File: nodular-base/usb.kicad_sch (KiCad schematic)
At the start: 39 parts, among them J10 Conn_01x02_MountingPin, J7 USB_C_Receptacle_USB2.0, J8 USB_C_Receptacle_USB2.0, U2 FUSB302BMPX, U29 RCLAMP0524P-ES, U3 BQ25895RTW, U43 TLV62595DMQR, U5 FUSB302BMPX, U50 TS3USB221A

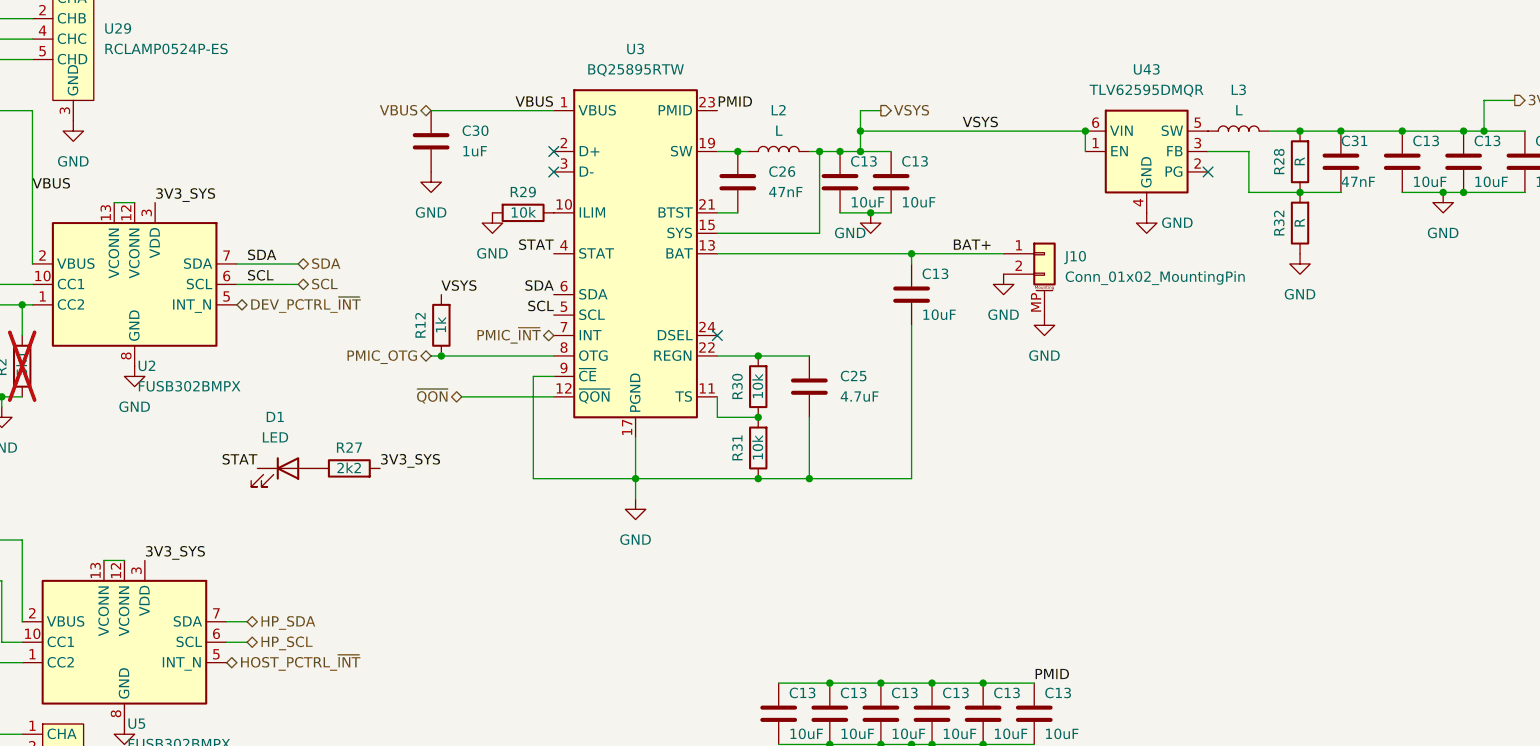
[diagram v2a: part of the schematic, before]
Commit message: Add hole Add decoupling caps, pullups, and voltage dividers Set current limit on PMIC Determine battery attachment angle Update BOM and pinouts
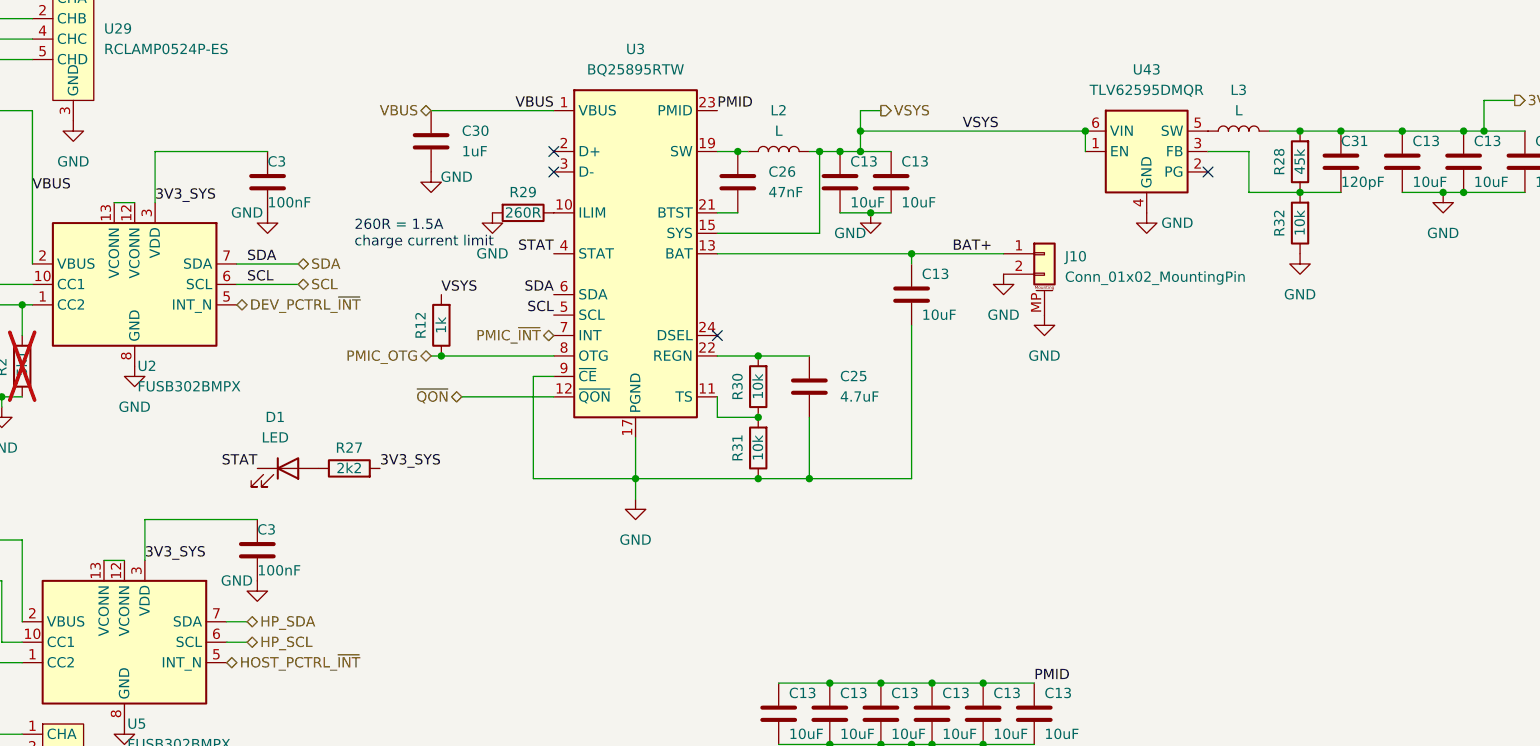
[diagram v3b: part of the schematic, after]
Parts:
- added C3 (x2): 100nF, Capacitor_SMD:C_0402_1005Metric, symbol Device:C
- C31: value 47nF -> 120pF
- J10: footprint JST_PH_B2B-PH-SM4-TB_1x02-1MP_P2.00mm_Vertical -> nodular:JST_PH_B2B-PH-SM4-TB_1x02-1MP_P2.00mm_Vertical
- R28: value R -> 45k
- R29: value 10k -> 260R
- R32: value R -> 10k
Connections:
- net 3V3_SYS: now also C3.1, C3.1
- net GND: now also C3.2, C3.2
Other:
- note added: "260R = 1.5A charge current limit"
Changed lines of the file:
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@@
+    (stroke (width 0) (type default))
+  )
+  (wire (pts (xy 109.22 39.37) (xy 95.25 39.37))
     (stroke (width 0) (type default))
   )
@@
     (stroke (width 0) (type default))
   )
+  (wire (pts (xy 107.95 85.09) (xy 93.98 85.09))
+    (stroke (width 0) (type default))
+  )
   (wire (pts (xy 172.72 113.03) (xy 179.07 113.03))
     (stroke (width 0) (type default))
@@
     (stroke (width 0) (type default))
   )
+  (wire (pts (xy 95.25 39.37) (xy 95.25 45.72))
+    (stroke (width 0) (type default))
+  )
   (wire (pts (xy 182.88 36.83) (xy 210.82 36.83))
     (stroke (width 0) (type default))
@@
     (stroke (width 0) (type default))
   )
+  (wire (pts (xy 93.98 85.09) (xy 93.98 90.17))
+    (stroke (width 0) (type default))
+  )
   (wire (pts (xy 78.74 87.63) (xy 78.74 97.79))
     (stroke (width 0) (type default))
@@
   (wire (pts (xy 107.95 140.97) (xy 110.49 140.97))
     (stroke (width 0) (type default))
+  )
+  (text "260R = 1.5A \ncharge current limit" (at 120.015 51.435 0)
+    (effects (font (size 1.27 1.27)) (justify left bottom))
   )
   (label "SDA" (at 144.78 57.15 180) (fields_autoplaced)
@@
   )
   (symbol (lib_id "power:GND") (at 129.54 41.91 0) (unit 1)
-    (in_bom yes) (on_board yes) (dnp no) (fields_autoplaced)
+    (in_bom yes) (on_board yes) (dnp no)
     (property "Reference" "#PWR045" (at 129.54 48.26 0)
       (effects (font (size 1.27 1.27)) hide)
     )
-    (property "Value" "GND" (at 129.54 46.99 0)
+    (property "Value" "GND" (at 132.715 42.545 0)
       (effects (font (size 1.27 1.27)))
     )
@@
     )
   )
+  (symbol (lib_id "Device:C") (at 109.22 43.18 0) (unit 1)
+    (in_bom yes) (on_board yes) (dnp no)
+    (property "Reference" "C3" (at 109.22 40.64 0)
+      (effects (font (size 1.27 1.27)) (justify left))
+    )
+    (property "Value" "100nF" (at 109.22 45.72 0)
+      (effects (font (size 1.27 1.27)) (justify left))
+    )
+    (property "Footprint" "Capacitor_SMD:C_0402_1005Metric" (at 110.1852 46.99 0)
+      (effects (font (size 1.27 1.27)) hide)
+    )
+    (property "Datasheet" "~" (at 109.22 43.18 0)
+      (effects (font (size 1.27 1.27)) hide)
+    )
+    (pin "1")
+    (pin "2")
+    (instances
+      (project "nodular-base"
+        (path "/6dcb0502-87e2-4c28-9ce8-81aab8925f06"
+          (reference "C3") (unit 1)
+        )
+        (path "/6dcb0502-87e2-4c28-9ce8-81aab8925f06/5ae693f9-48f3-406c-bbdf-b76d81cc71eb"
+          (reference "C16") (unit 1)
+        )
+        (path "/6dcb0502-87e2-4c28-9ce8-81aab8925f06/52c49487-f3d5-40e2-8f19-e7b81498d838"
+          (reference "C44") (unit 1)
+        )
+        (path "/6dcb0502-87e2-4c28-9ce8-81aab8925f06/febeaf27-8aaa-445d-863a-3f8ee5c51d55"
+          (reference "C46") (unit 1)
+        )
+      )
+    )
+  )
+  (symbol (lib_id "power:GND") (at 107.95 92.71 0) (unit 1)
+    (in_bom yes) (on_board yes) (dnp no)
+    (property "Reference" "#PWR064" (at 107.95 99.06 0)
+      (effects (font (size 1.27 1.27)) hide)
+    )
+    (property "Value" "GND" (at 105.41 92.71 0)
+      (effects (font (size 1.27 1.27)))
+    )
+    (property "Footprint" "" (at 107.95 92.71 0)
+      (effects (font (size 1.27 1.27)) hide)
+    )
+    (property "Datasheet" "" (at 107.95 92.71 0)
+      (effects (font (size 1.27 1.27)) hide)
+    )
+    (pin "1")
+    (instances
+      (project "nodular-base"
+        (path "/6dcb0502-87e2-4c28-9ce8-81aab8925f06/52c49487-f3d5-40e2-8f19-e7b81498d838"
+          (reference "#PWR064") (unit 1)
+        )
+        (path "/6dcb0502-87e2-4c28-9ce8-81aab8925f06/febeaf27-8aaa-445d-863a-3f8ee5c51d55"
+          (reference "#PWR067") (unit 1)
+        )
+      )
+    )
+  )
   (symbol (lib_id "Device:C") (at 167.64 43.18 0) (unit 1)
     (in_bom yes) (on_board yes) (dnp no) (fields_autoplaced)
@@
       (effects (font (size 1.27 1.27)))
     )
-    (property "Value" "10k" (at 140.97 46.99 90)
+    (property "Value" "260R" (at 140.97 46.99 90)
       (effects (font (size 1.27 1.27)))
     )
@@
       (effects (font (size 1.27 1.27)) (justify left))
     )
-    (property "Footprint" "JST_PH_B2B-PH-SM4-TB_1x02-1MP_P2.00mm_Vertical" (at 205.74 52.07 0)
+    (property "Footprint" "nodular:JST_PH_B2B-PH-SM4-TB_1x02-1MP_P2.00mm_Vertical" (at 205.74 52.07 0)
       (effects (font (size 1.27 1.27)) hide)
     )
@@
         (path "/6dcb0502-87e2-4c28-9ce8-81aab8925f06/febeaf27-8aaa-445d-863a-3f8ee5c51d55"
           (reference "L2") (unit 1)
+        )
+      )
+    )
+  )
+  (symbol (lib_id "Device:C") (at 107.95 88.9 0) (unit 1)
+    (in_bom yes) (on_board yes) (dnp no)
+    (property "Reference" "C3" (at 107.95 86.36 0)
+      (effects (font (size 1.27 1.27)) (justify left))
+    )
+    (property "Value" "100nF" (at 107.95 91.44 0)
+      (effects (font (size 1.27 1.27)) (justify left))
+    )
+    (property "Footprint" "Capacitor_SMD:C_0402_1005Metric" (at 108.9152 92.71 0)
+      (effects (font (size 1.27 1.27)) hide)
+    )
+    (property "Datasheet" "~" (at 107.95 88.9 0)
+      (effects (font (size 1.27 1.27)) hide)
+    )
+    (pin "1")
+    (pin "2")
+    (instances
+      (project "nodular-base"
+        (path "/6dcb0502-87e2-4c28-9ce8-81aab8925f06"
+          (reference "C3") (unit 1)
+        )
+        (path "/6dcb0502-87e2-4c28-9ce8-81aab8925f06/5ae693f9-48f3-406c-bbdf-b76d81cc71eb"
+          (reference "C16") (unit 1)
+        )
+        (path "/6dcb0502-87e2-4c28-9ce8-81aab8925f06/52c49487-f3d5-40e2-8f19-e7b81498d838"
+          (reference "C44") (unit 1)
+        )
+        (path "/6dcb0502-87e2-4c28-9ce8-81aab8925f06/febeaf27-8aaa-445d-863a-3f8ee5c51d55"
+          (reference "C47") (unit 1)
         )
       )
@@
       (effects (font (size 1.27 1.27)))
     )
-    (property "Value" "R" (at 237.49 40.64 90)
+    (property "Value" "45k" (at 237.49 40.64 90)
       (effects (font (size 1.27 1.27)))
     )
@@
       (effects (font (size 1.27 1.27)))
     )
-    (property "Value" "R" (at 237.49 48.26 90)
+    (property "Value" "10k" (at 237.49 48.26 90)
       (effects (font (size 1.27 1.27)))
     )
@@
     )
   )
+  (symbol (lib_id "power:GND") (at 109.22 46.99 0) (unit 1)
+    (in_bom yes) (on_board yes) (dnp no)
+    (property "Reference" "#PWR064" (at 109.22 53.34 0)
+      (effects (font (size 1.27 1.27)) hide)
+    )
+    (property "Value" "GND" (at 106.68 46.99 0)
+      (effects (font (size 1.27 1.27)))
+    )
+    (property "Footprint" "" (at 109.22 46.99 0)
+      (effects (font (size 1.27 1.27)) hide)
+    )
+    (property "Datasheet" "" (at 109.22 46.99 0)
+      (effects (font (size 1.27 1.27)) hide)
+    )
+    (pin "1")
+    (instances
+      (project "nodular-base"
+        (path "/6dcb0502-87e2-4c28-9ce8-81aab8925f06/52c49487-f3d5-40e2-8f19-e7b81498d838"
+          (reference "#PWR064") (unit 1)
+        )
+        (path "/6dcb0502-87e2-4c28-9ce8-81aab8925f06/febeaf27-8aaa-445d-863a-3f8ee5c51d55"
+          (reference "#PWR066") (unit 1)
+        )
+      )
+    )
+  )
   (symbol (lib_id "Device:C") (at 265.43 40.64 0) (unit 1)
     (in_bom yes) (on_board yes) (dnp no)
@@
       (effects (font (size 1.27 1.27)) (justify left))
     )
-    (property "Value" "47nF" (at 242.57 43.18 0)
-      (effects (font (size 1.27 1.27)) (justify left))
-    )
+    (property "Value" "120pF" (at 242.57 43.18 0)
+      (effects (font (size 1.27 1.27)) (justify left))
+    )

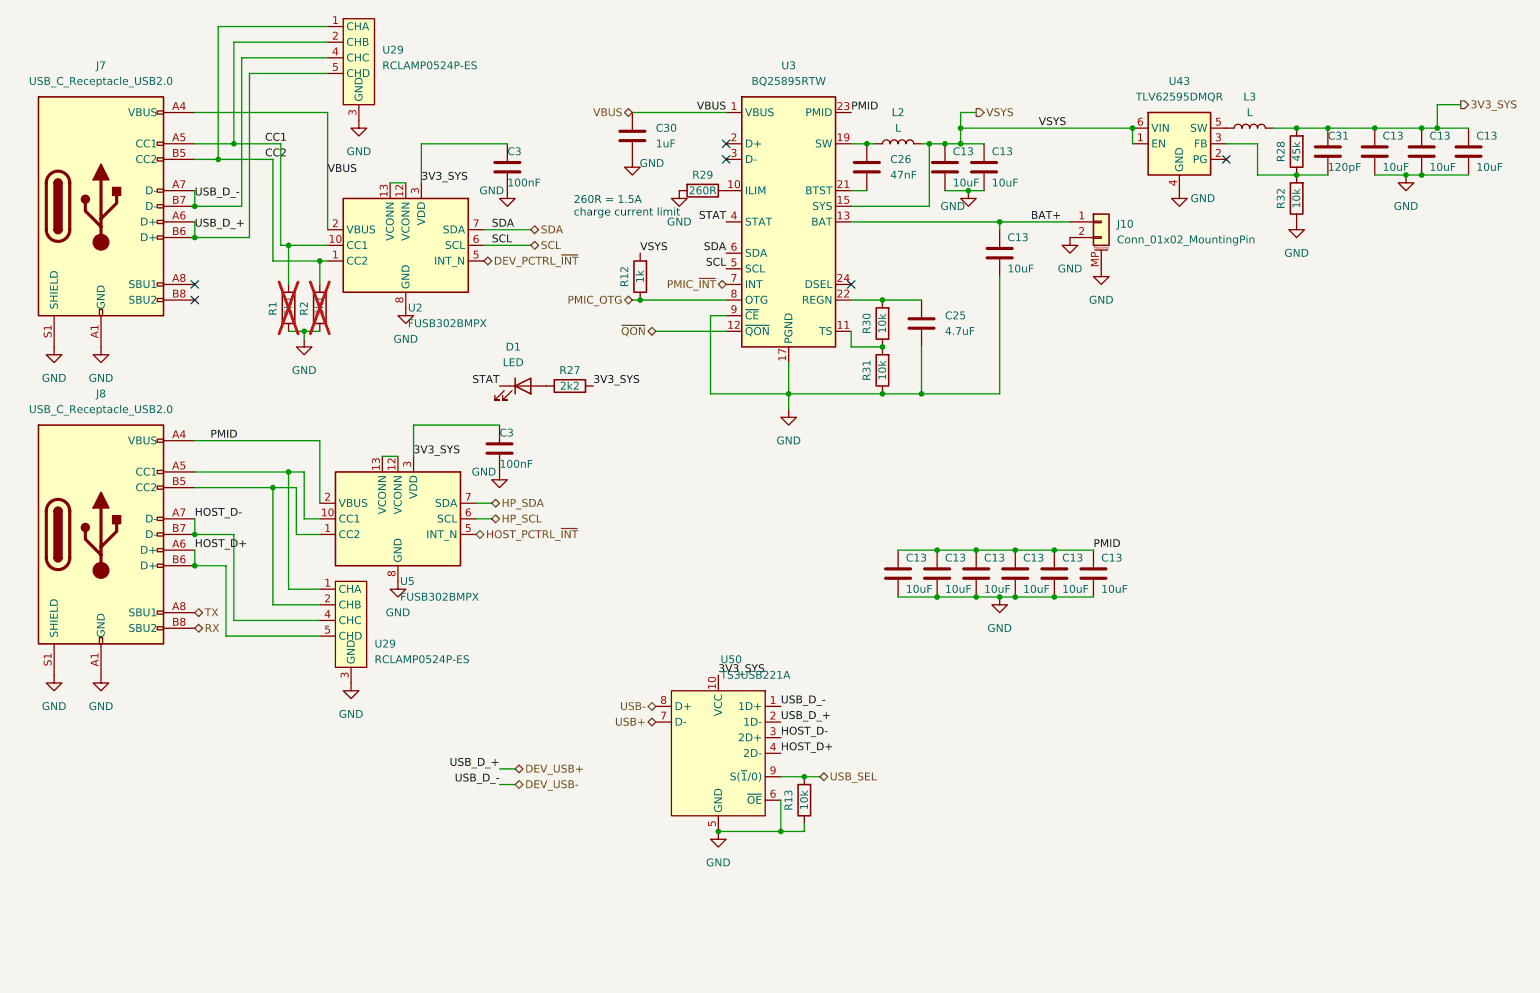
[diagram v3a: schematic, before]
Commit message: Add VCONN support and load switch with 1.5A current limit on host port Add accelerometer interrupt connection Update BOM with important capacitor and inductor PNs and costings
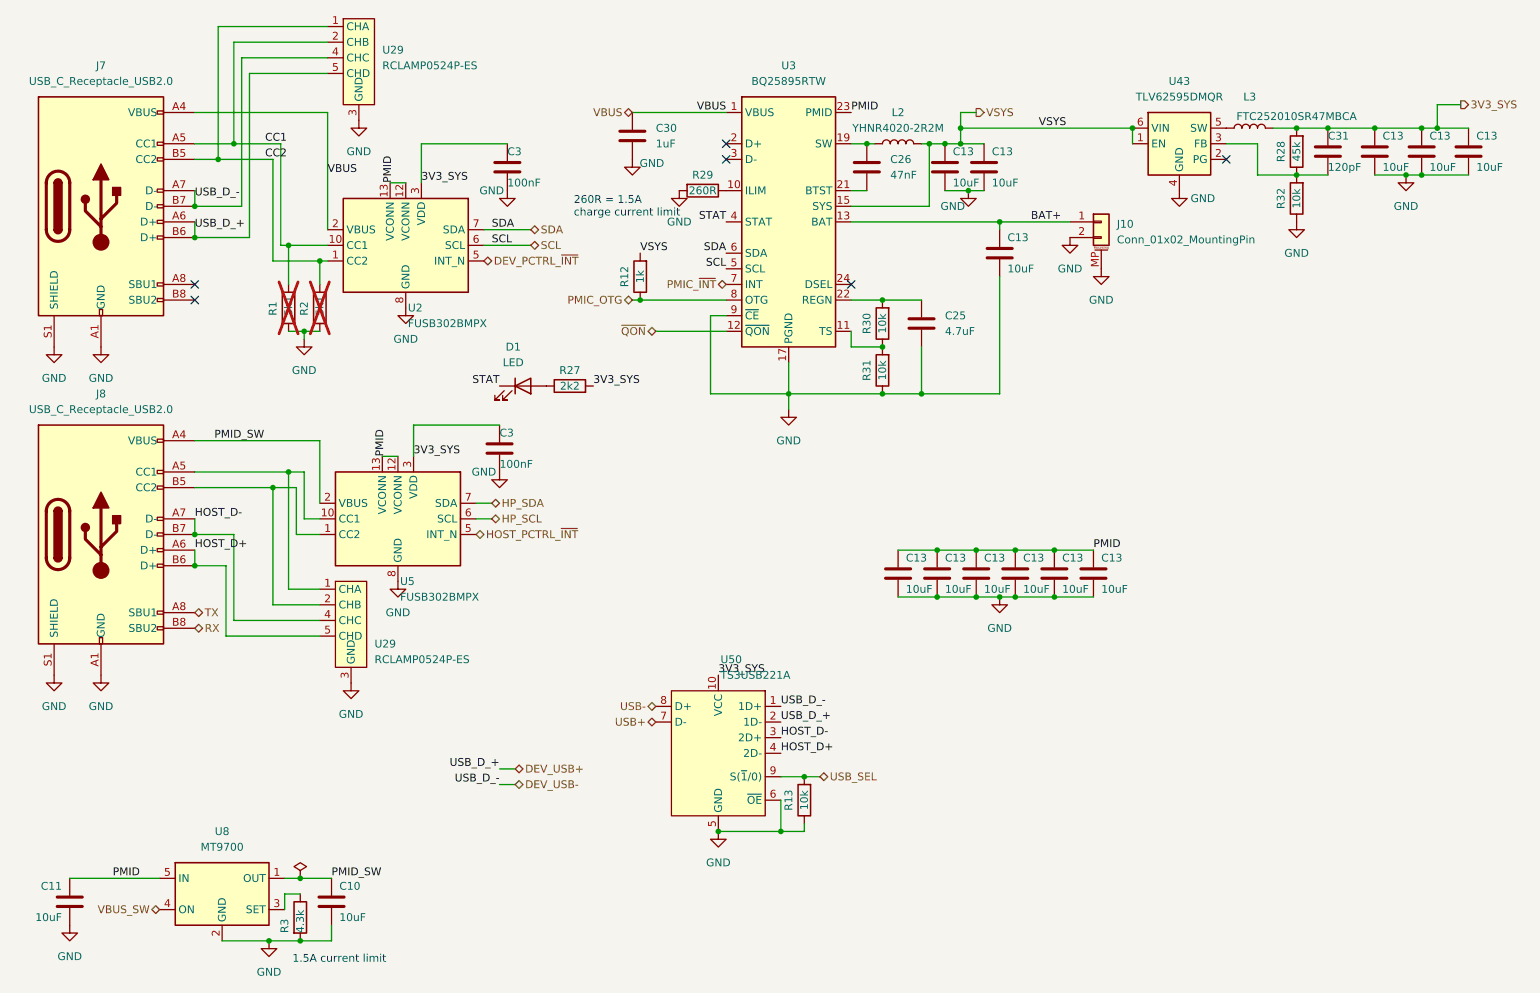
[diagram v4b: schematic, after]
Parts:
- added C10, C11: 10uF, Capacitor_SMD:C_1206_3216Metric, symbol Device:C
- added R3: 4.3k, Resistor_SMD:R_0402_1005Metric, symbol Device:R
- added U8: MT9700, Package_TO_SOT_SMD:SOT-23-5, symbol Power_Management:AAT4610BIGV-1-T1
- L2: value L -> YHNR4020-2R2M
- L3: value L -> FTC252010SR47MBCA
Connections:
- net GND: now also C10.2, C11.2, R3.2, U8.2 (GND)
- net PMID: now also U2.12 (VCONN), U2.13 (VCONN), U5.12 (VCONN), U5.13 (VCONN), C11.1, U8.5 (IN); no longer J8.A4 (VBUS), J8.A9 (VBUS), J8.B4 (VBUS), J8.B9 (VBUS), U5.2 (VBUS)
- new net: R3.1, U8.3 (SET)
- new net PMID_SW: C10.1, J8.A4 (VBUS), J8.A9 (VBUS), J8.B4 (VBUS), J8.B9 (VBUS), U5.2 (VBUS), U8.1 (OUT)
- new net VBUS_SW: U8.4 (ON)
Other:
- note added: "1.5A current limit"
